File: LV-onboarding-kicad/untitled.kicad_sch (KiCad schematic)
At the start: 1 part, among them K1 Relay_SPST-NO

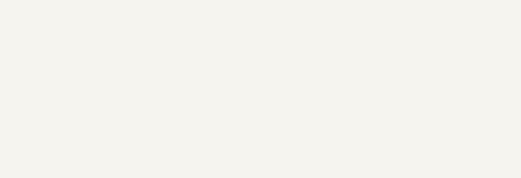
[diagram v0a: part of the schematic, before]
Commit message: worked in BSPD
checked the datasheet for HASS sensor and made a low pass filter in LTSpice
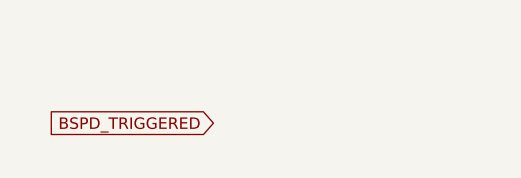
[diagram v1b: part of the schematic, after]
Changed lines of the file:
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@@
 		(comment 1 "Charles Ge")
+	)
+	(global_label "BSPD_TRIGGERED"
+		(shape input)
+		(at 83.82 91.44 180)
+		(fields_autoplaced yes)
+		(effects
+			(font
+				(size 1.27 1.27)
+			)
+			(justify right)
+		)
+		(property "Intersheetrefs" "${INTERSHEET_REFS}"
+			(at 64.6273 91.44 0)
+			(hide yes)
+			(show_name no)
+			(do_not_autoplace no)
+			(effects
+				(font
+					(size 1.27 1.27)
+				)
+				(justify right)
+			)
+		)
 	)
 	(symbol

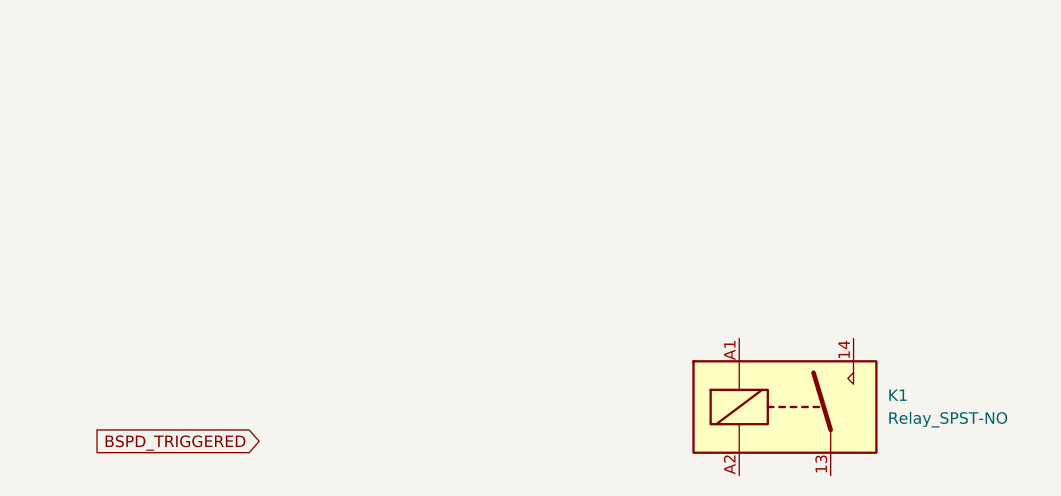
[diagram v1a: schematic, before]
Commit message: fixed logic in BSPD
changed NAND gates to NOT and AND gates
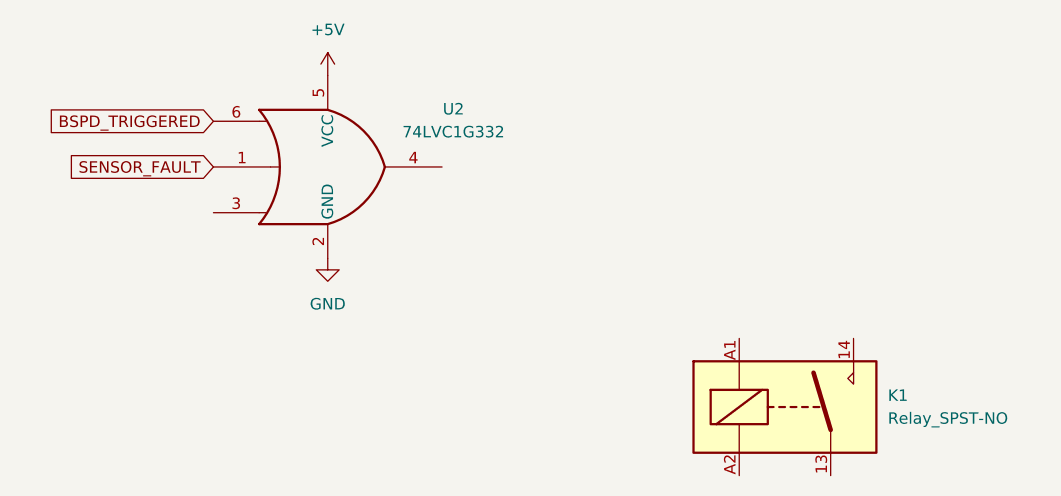
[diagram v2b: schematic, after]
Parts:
- added U2: 74LVC1G332, Package_TO_SOT_THT:TO-220-2_Vertical, symbol 74xGxx:74LVC1G332
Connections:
- net BSPD_TRIGGERED: now also U2.6
- new net +5V: U2.5 (VCC)
- new net GND: U2.2 (GND)
- new net SENSOR_FAULT: U2.1
